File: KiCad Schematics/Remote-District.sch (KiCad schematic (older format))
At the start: 23 parts, among them M1 Fan

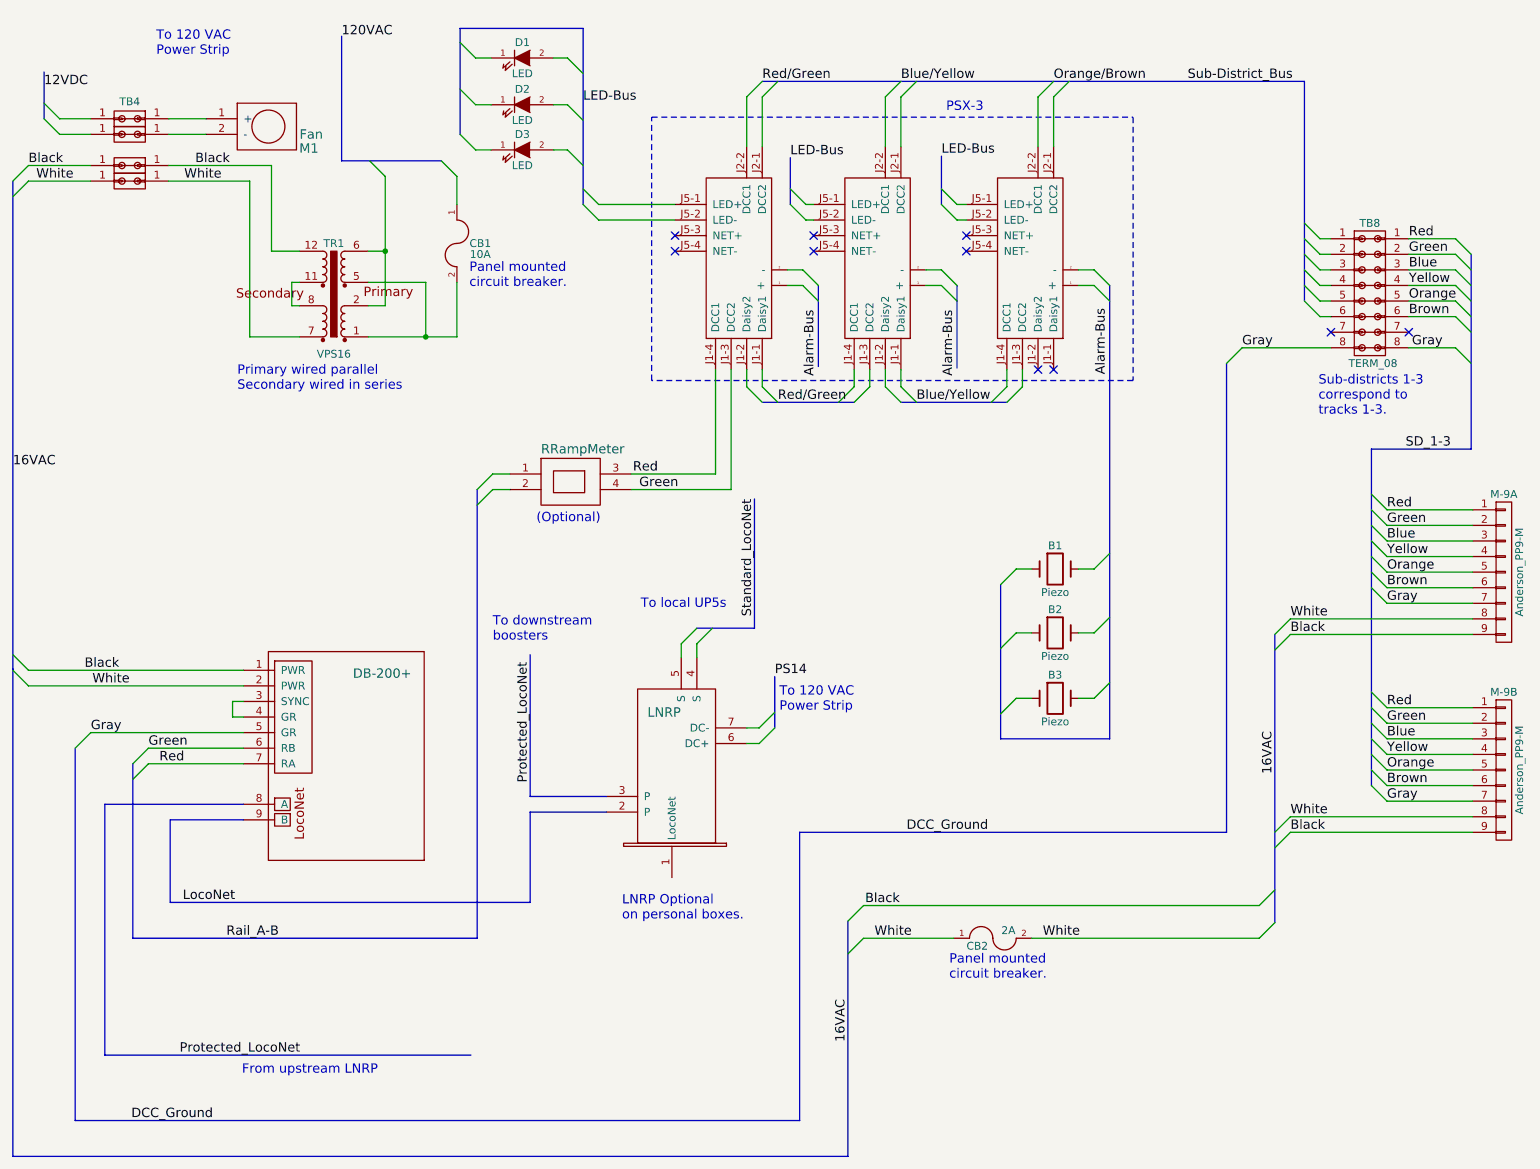
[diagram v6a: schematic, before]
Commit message: Simplified schematic
Added heirarchy sheets to simplify the schematic.
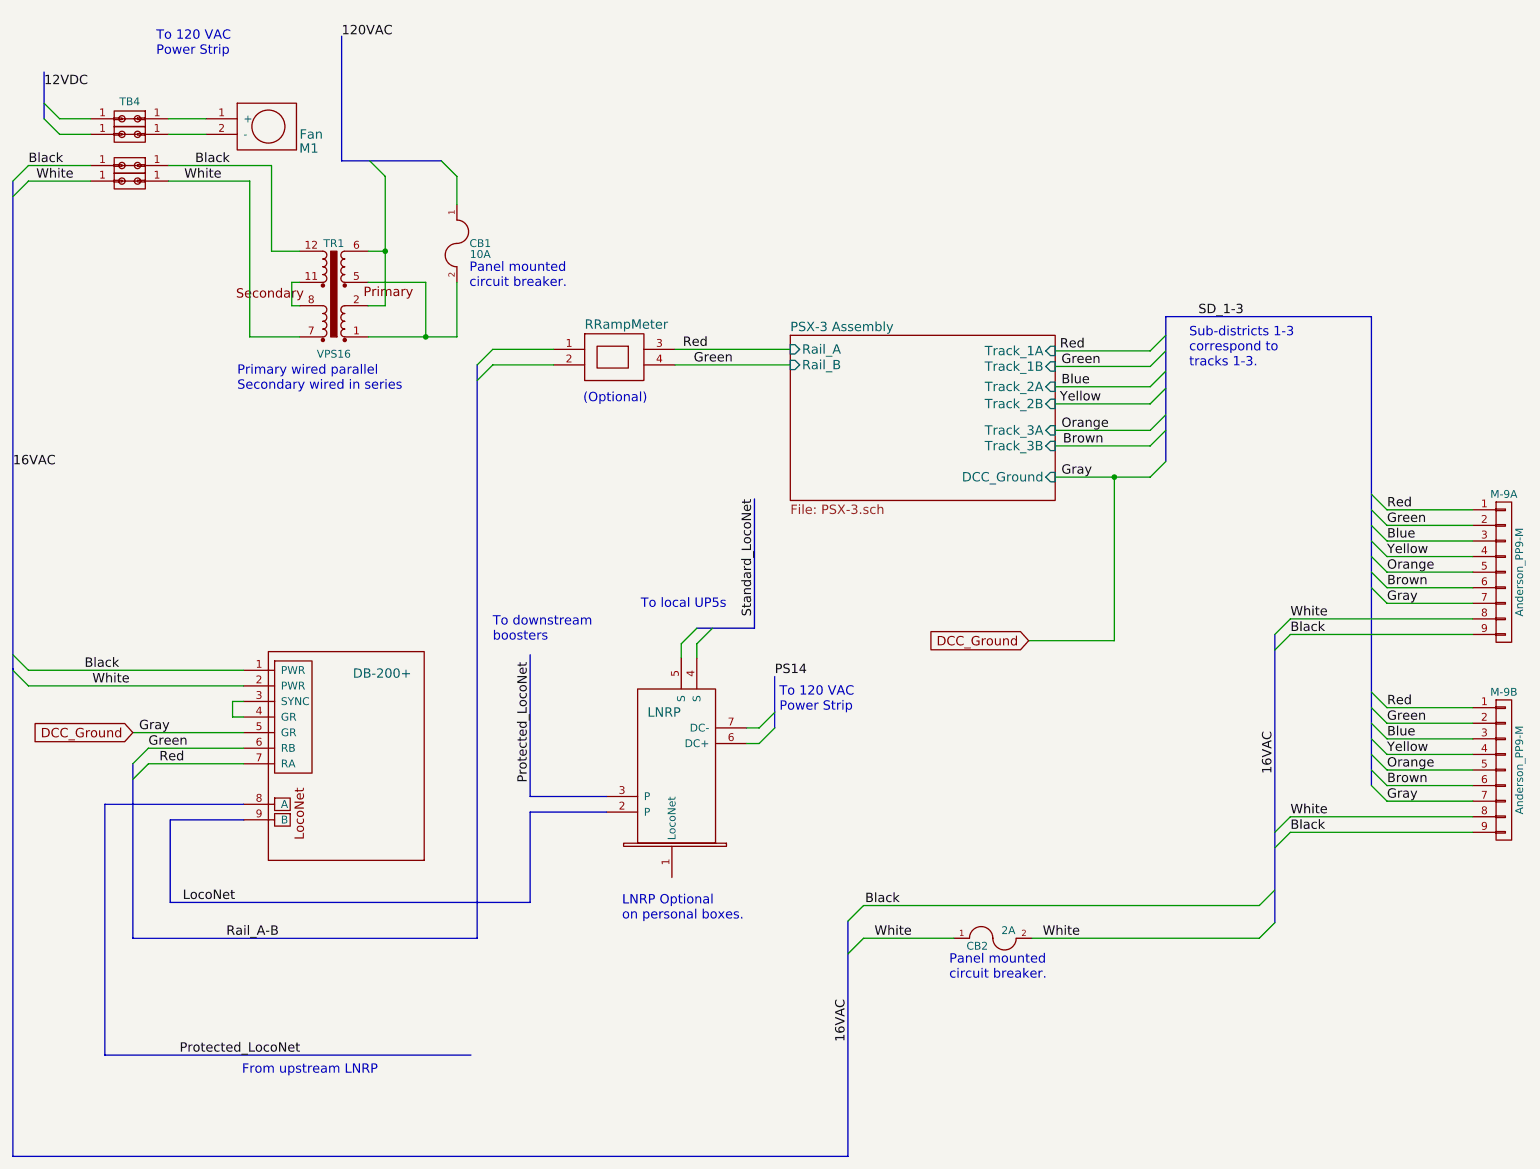
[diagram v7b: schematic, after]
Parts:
- removed B1, B2, B3: Piezo, symbol Crystal
- removed D1, D2, D3: LED, symbol LED
- removed PSX?: PSX-4, symbol PSX
- removed PSX? (x2): PSX, symbol PSX
- removed TB8: TERM_08, symbol TERM_08
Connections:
- net Gray is gone; now on net DCC_Ground: DB?.5 (GR), M-9A.7 (P7), M-9B.7 (P7)
- no-connect marks 10 -> 0
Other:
- note removed: "PSX-3"

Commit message: Corrected transformer wire colors
Corrected error in Triad transformer colors to match black to 'hot' and
white to 'neutral'.
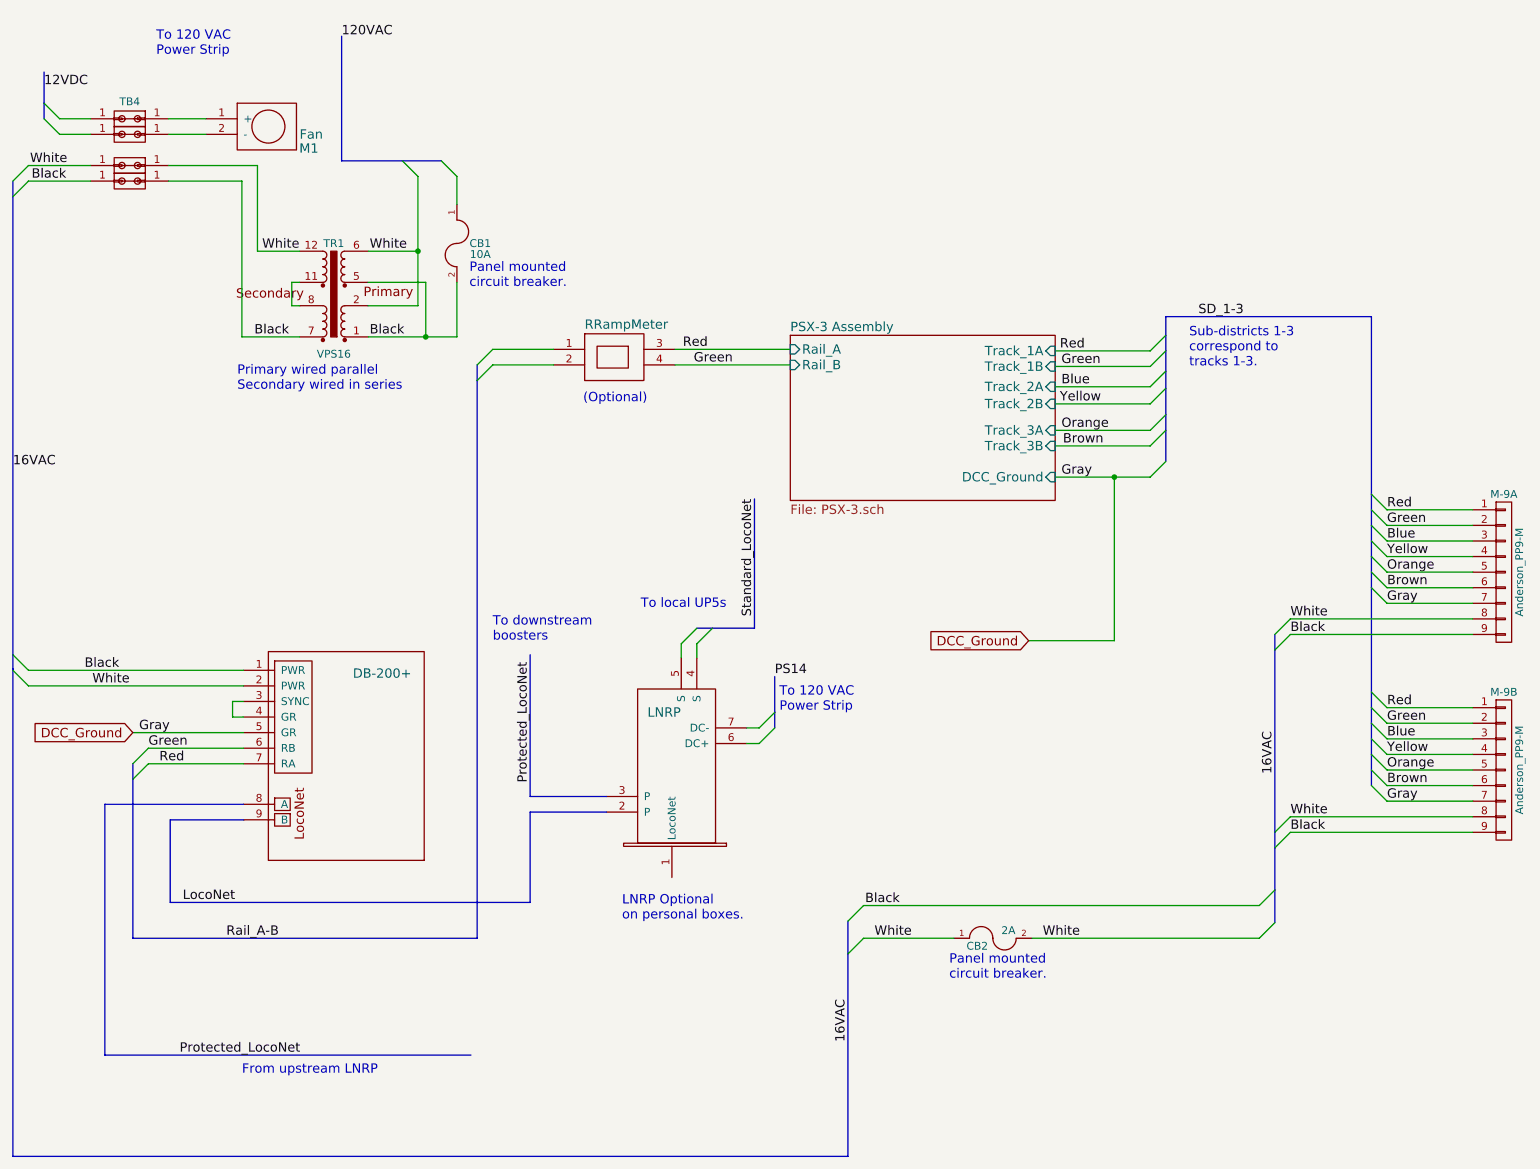
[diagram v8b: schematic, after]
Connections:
- net Black: now also CB1.2, TB?.1 (P1), TR1.1, TR1.5, TR1.7; no longer TB?.1 (P1), TR1.12
- net White: now also TB?.1 (P1), TR1.12, TR1.2, TR1.6; no longer TB?.1 (P1), TR1.7
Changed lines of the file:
@@
 	1050 1250 850  1250
 Wire Bus Line
-	750  850  750  1150
+	750  850  750  1050
+Wire Bus Line
+	750  1050 750  1150
 Wire Wire Line
 	1050 1450 650  1450
@@
 	2030 5290 1420 5290
 Wire Bus Line
-	1320 5290 1320 6410
+	1320 5290 1320 5390
+Wire Bus Line
+	1320 5390 1320 6410
 Wire Bus Line
 	2030 5650 1560 5650
@@
 	5340 5160 5440 5060
 Wire Bus Line
-	5440 4730 5440 5060
+	5440 4730 5440 4960
+Wire Bus Line
+	5440 4960 5440 5060
 Text Label 5440 4730 0    60   ~ 0
 PS14
@@
 16VAC
 Wire Bus Line
-	3530 6410 3530 2730
-Wire Bus Line
-	550  1550 550  7810
+	3530 6410 3530 2830
+Wire Bus Line
+	3530 2830 3530 2730
+Wire Bus Line
+	550  1550 550  1650
+Wire Bus Line
+	550  1650 550  4590
+Wire Bus Line
+	550  4590 550  4690
+Wire Bus Line
+	550  4690 550  7810
 Text Notes 1990 2900 0    60   ~ 0
 Primary wired parallel\nSecondary wired in series
@@
 Sub-districts 1-3\ncorrespond to\ntracks 1-3.
 Wire Bus Line
-	4940 4420 5310 4420
+	4940 4420 5040 4420
+Wire Bus Line
+	5040 4420 5310 4420
 Wire Bus Line
 	5310 4420 5310 3590
@@
 	5910 6300 6010 6200
 Wire Bus Line
-	5910 6300 5910 7810
+	5910 6300 5910 6510
+Wire Bus Line
+	5910 6510 5910 7810
 Text Label 5910 6800 3    60   ~ 0
 16VAC
@@
 	2340 2200 2390 2200
 Wire Wire Line
-	2210 2000 2390 2000
-Wire Wire Line
-	2070 2550 2390 2550
-Wire Wire Line
-	1550 1450 2210 1450
-Wire Wire Line
-	2210 1450 2210 2000
-Wire Wire Line
-	1550 1550 2070 1550
-Wire Wire Line
-	2070 1550 2070 2550
+	2120 2000 2390 2000
+Wire Wire Line
+	2020 2550 2390 2550
+Wire Wire Line
+	1550 1450 2120 1450
+Wire Wire Line
+	2120 1450 2120 2000
+Wire Wire Line
+	1550 1550 2020 1550
+Wire Wire Line
+	2020 1550 2020 2550
 Wire Wire Line
 	1550 1150 1790 1150
@@
 	3300 1420 3400 1520
 Entry Wire Line
-	2840 1420 2940 1520
-Wire Bus Line
-	2660 1420 3300 1420
+	3050 1420 3150 1520
+Wire Bus Line
+	2660 1420 3050 1420
+Wire Bus Line
+	3050 1420 3300 1420
 Wire Bus Line
 	2660 1420 2660 620
@@
 Text Label 1060 4790 0    60   ~ 0
 White
-Text Label 650  1450 0    60   ~ 0
-Black
-Text Label 700  1550 0    60   ~ 0
-White
-Text Label 1650 1550 0    60   ~ 0
-White
-Text Label 1720 1450 0    60   ~ 0
+Text Label 670  1550 0    60   ~ 0
+Black
+Text Label 660  1450 0    60   ~ 0
+White
+Text Label 2150 2000 0    60   ~ 0
+White
+Text Label 2100 2550 0    60   ~ 0
 Black
 Text Label 6020 6200 0    60   ~ 0
@@
 $EndComp
 Wire Wire Line
-	2940 2350 2830 2350
-Wire Wire Line
-	2940 1520 2940 2350
-Wire Wire Line
-	2830 2000 2940 2000
-Connection ~ 2940 2000
+	3150 2350 2830 2350
+Wire Wire Line
+	3150 1520 3150 2000
+Wire Wire Line
+	3150 2000 3150 2350
+Wire Wire Line
+	2830 2000 3150 2000
+Wire Wire Line
+	3150 2000 3150 2000
+Connection ~ 3150 2000
 Wire Wire Line
 	3400 1520 3400 1700
@@
 	3400 2550 3400 2200
 Wire Wire Line
-	2830 2550 3400 2550
+	2830 2550 3200 2550
+Wire Wire Line
+	3200 2550 3400 2550
 Wire Wire Line
 	2830 2200 3200 2200
@@
 $EndComp
 Wire Bus Line
-	9270 2420 9270 5430
+	9270 2420 9270 3560
+Wire Bus Line
+	9270 3560 9270 3660
+Wire Bus Line
+	9270 3660 9270 3760
+Wire Bus Line
+	9270 3760 9270 3860
+Wire Bus Line
+	9270 3860 9270 3960
+Wire Bus Line
+	9270 3960 9270 4060
+Wire Bus Line
+	9270 4060 9270 4160
+Wire Bus Line
+	9270 4160 9270 4830
+Wire Bus Line
+	9270 4830 9270 4930
+Wire Bus Line
+	9270 4930 9270 5030
+Wire Bus Line
+	9270 5030 9270 5130
+Wire Bus Line
+	9270 5130 9270 5230
+Wire Bus Line
+	9270 5230 9270 5330
+Wire Bus Line
+	9270 5330 9270 5430
 Entry Wire Line
 	8650 4560 8750 4460
@@
 	8650 5730 8750 5630
 Wire Bus Line
-	8650 4460 8650 6310
+	8650 4460 8650 4560
+Wire Bus Line
+	8650 4560 8650 5730
+Wire Bus Line
+	8650 5730 8650 5830
+Wire Bus Line
+	8650 5830 8650 6100
+Wire Bus Line
+	8650 6100 8650 6310
 Text Label 9370 3660 0    60   ~ 0
 Red
@@
 Brown
 Wire Wire Line
-	7240 3450 7850 3450
+	7240 3450 7620 3450
+Wire Wire Line
+	7620 3450 7850 3450
 Entry Wire Line
 	7850 3450 7950 3350
@@
 Gray
 Wire Bus Line
-	7950 2420 7950 3350
+	7950 2420 7950 2540
+Wire Bus Line
+	7950 2540 7950 2640
+Wire Bus Line
+	7950 2640 7950 2770
+Wire Bus Line
+	7950 2770 7950 2880
+Wire Bus Line
+	7950 2880 7950 3050
+Wire Bus Line
+	7950 3050 7950 3150
+Wire Bus Line
+	7950 3150 7950 3350
 Wire Bus Line
 	7950 2420 9270 2420
@@
 	7620 4500 7070 4500
 Connection ~ 7620 3450
+Text Label 2840 2550 0    60   ~ 0
+Black
+Text Label 2840 2000 0    60   ~ 0
+White
 $EndSCHEMATC
